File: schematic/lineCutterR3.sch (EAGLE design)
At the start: 53 parts, among them IC2 MC33269ST-3.3T3, J1 10118192-0001LF, Q1 AO4576, Q2 AO4576, Q3 DMG2305, Q4 AO4576, SW1 KMR2, U1 MS560702BA03-50, U2 MDBT50Q, U3 S25FL128SDPMFIG13S03016, U4 ESP32-S2-WROVER, U5 KXTJ3-1057, X1 2x5 0.05", X2 PIN-HEADER-MICRO-2-5-SMD

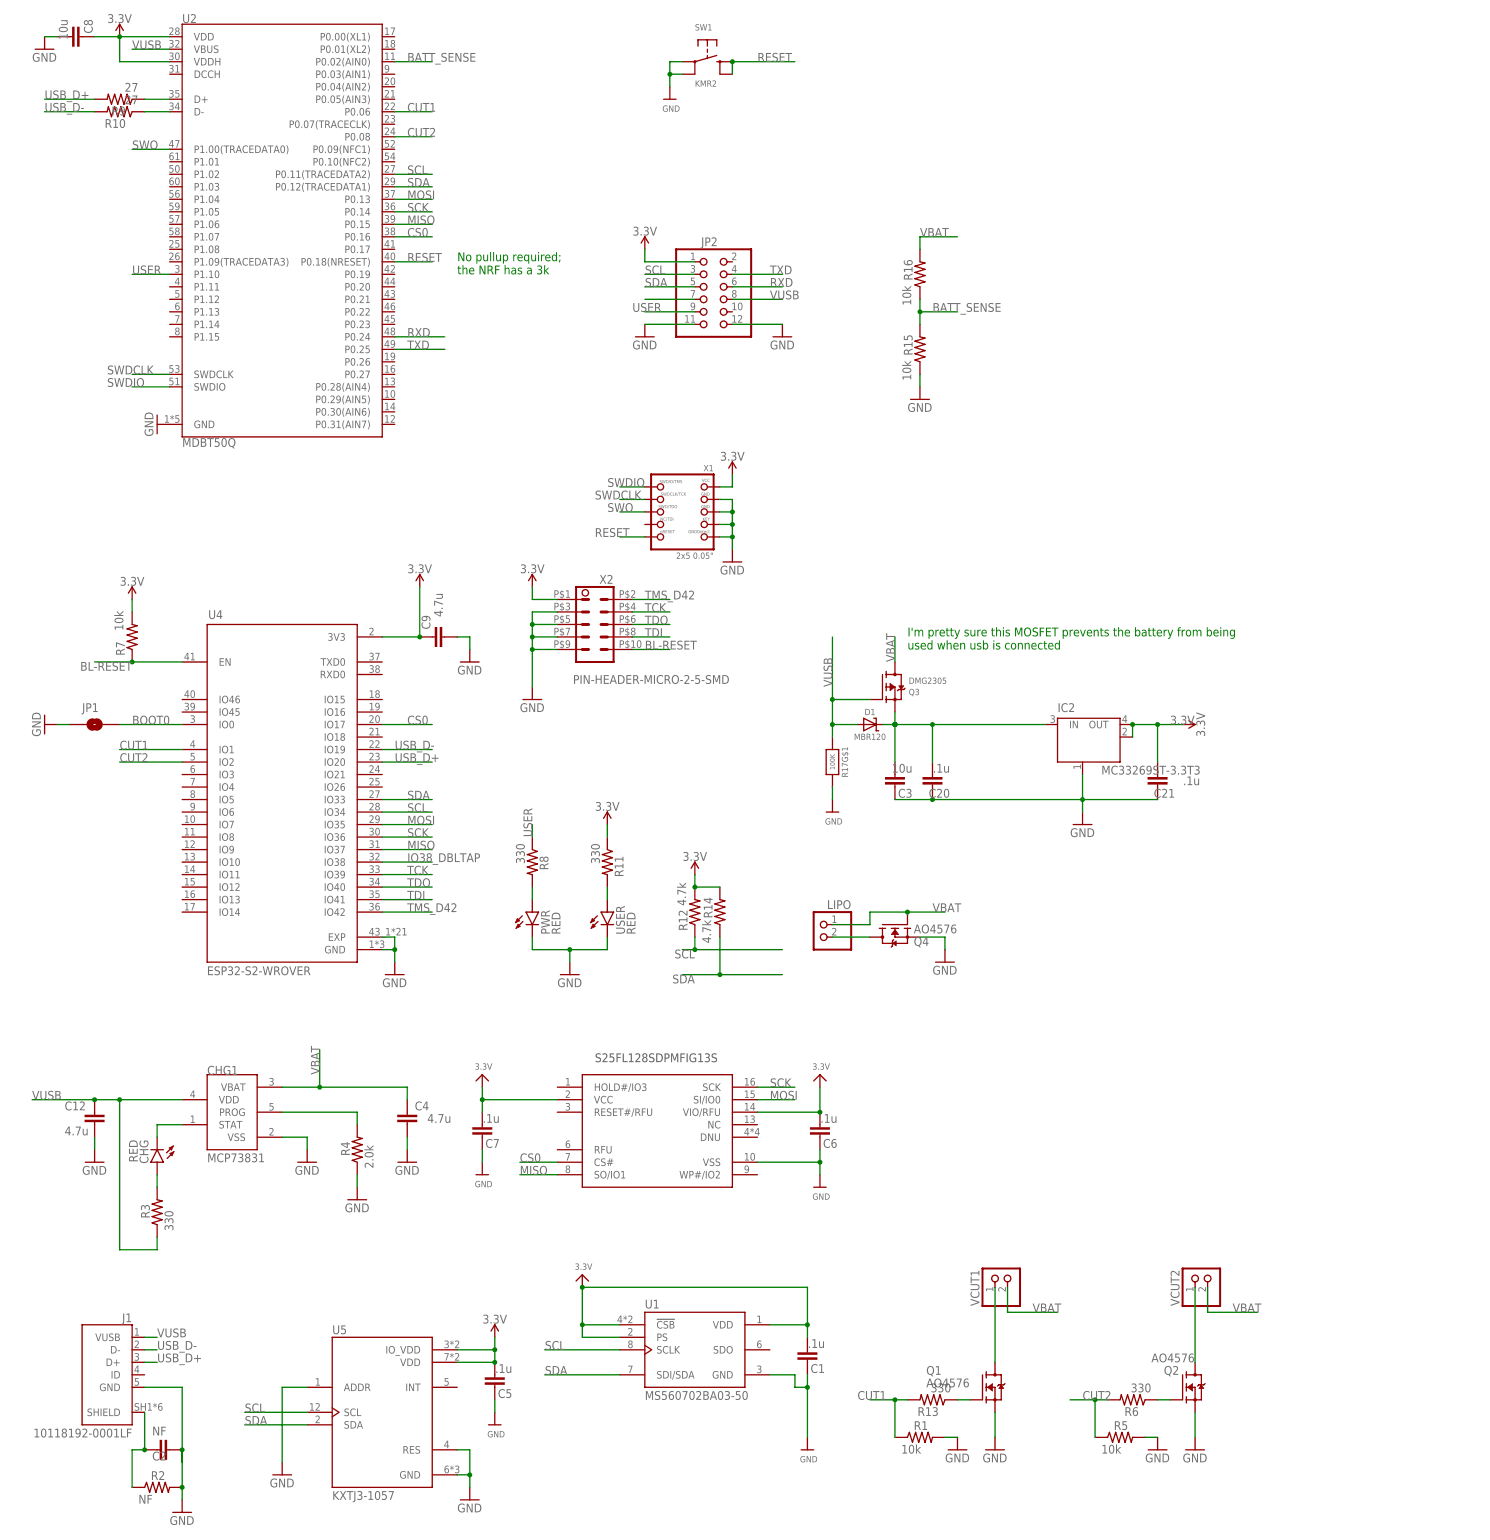
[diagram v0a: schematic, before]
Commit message: Add Buck/Boost, RGB, Continuity, current sense
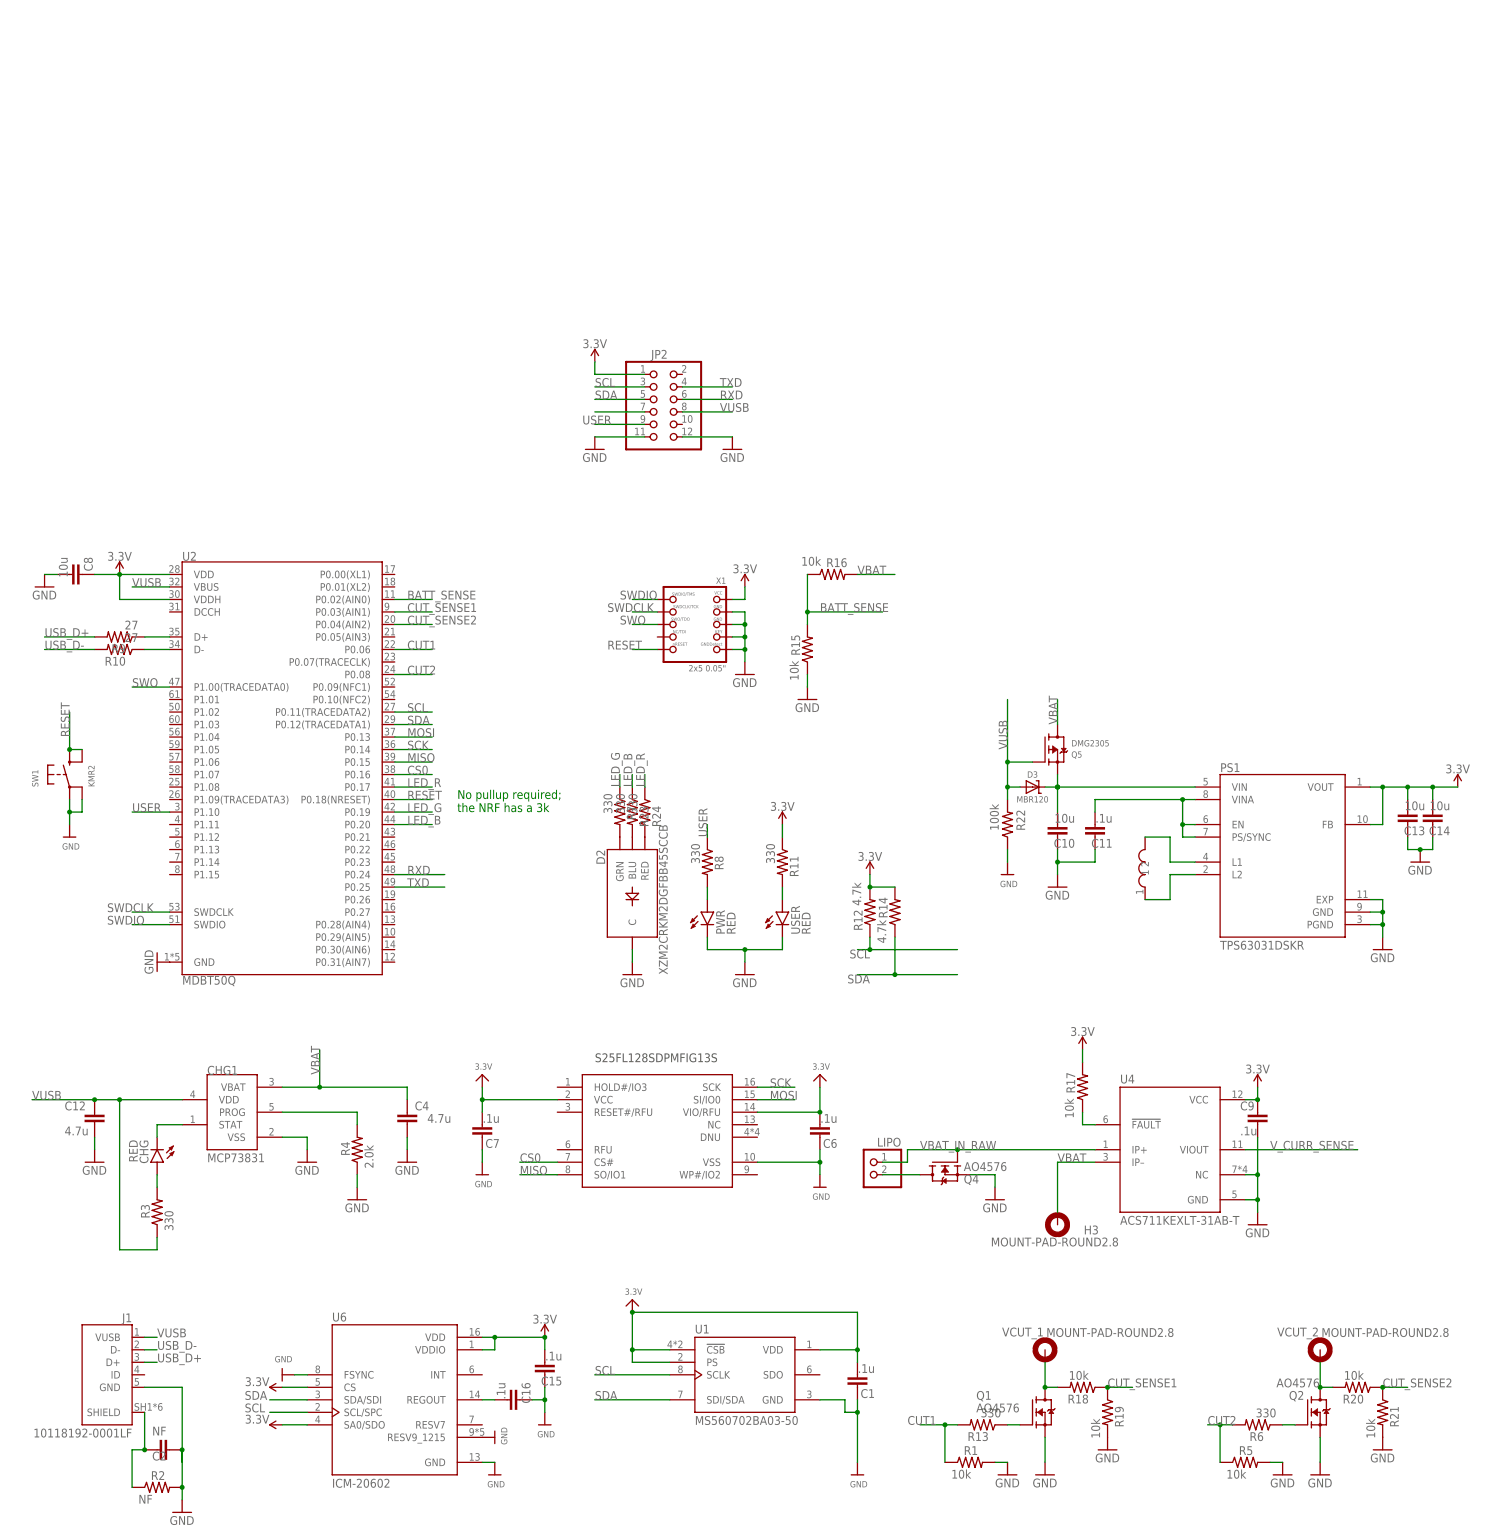
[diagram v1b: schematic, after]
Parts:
- removed C20, C21, C5: .1u, rcl:C-EUC0805
- removed C3: 10u, rcl:C-EUC0805
- removed D1: MBR120, microbuilder:DIODE-SCHOTTKYSOD-123
- removed IC2: MC33269ST-3.3T3, linear:MC33269ST-3.3T3
- removed JP1: JUMPER-SMT_2_NO_SILK, SparkFun-Jumpers:JUMPER-SMT_2_NO_SILK
- removed Q3: DMG2305, microbuilder:MOSFET-P
- removed U5: KXTJ3-1057, Line Cutter COTS:KXTJ3-1057
- removed VCUT1, VCUT2: (no value), pinhead:PINHD-1X2
- removed X2: PIN-HEADER-MICRO-2-5-SMD, freescale-uc:PIN-HEADER-MICRO-2-5-SMD
- added C10, C13, C14: 10u, rcl:C-EUC0805
- added C11, C15, C16: .1u, rcl:C-EUC0805
- added D2: XZM2CRKM2DGFBB45SCCB, SparkFun-LED:SUNLEDSMD1
- added D3: MBR120, microbuilder:DIODE-SCHOTTKYSOD-123
- added H3, VCUT_1, VCUT_2: MOUNT-PAD-ROUND2.8, holes:MOUNT-PAD-ROUND2.8
- added L1: NR3015T1R5N, Line Cutter COTS:NR3015T1R5N
- added PS1: TPS63031DSKR, Line Cutter COTS:TPS63031DSKR
- added Q5: DMG2305, microbuilder:MOSFET-P
- added R18, R19, R20, R21: 10k, rcl:R-US_R0805
- added R22: 100k, rcl:R-US_R0805
- added R23, R24: 330, rcl:R-US_R0805
- added U6: ICM-20602, Line Cutter COTS:ICM-20602
- C9: value 4.7u -> .1u
- R17: value 100K -> 10k; device microbuilder:RESISTOR_4PACK -> rcl:R-US_R0805
- R7: value 10k -> 330
- U4: value ESP32-S2-WROVER -> ACS711KEXLT-31AB-T; device Line Cutter COTS:ESP32-S2-WROVER -> Line Cutter COTS:ACS711KEXLT-31AB-T
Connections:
- removed net BL-RESET: R7.1, U4.EN, X2.10
- removed net BOOT0: JP1.2, U4.IO0
- removed net IO38_DBLTAP: U4.IO38
- removed net TCK: U4.IO39, X2.4
- removed net TDI: U4.IO41, X2.8
- removed net TDO: U4.IO40, X2.6
- removed net TMS_D42: U4.IO42, X2.2
- removed net VHI: C20.2, C3.2, D1.C, IC2.IN, Q3.S
- new net CUT_SENSE1: R18.1, R19.1, U2.P0.03(AIN1)
- new net CUT_SENSE2: R20.1, R21.1, U2.P0.04(AIN2)
- new net LED_B: R23.1, U2.P0.20
- new net LED_G: R7.1, U2.P0.19
- new net LED_R: R24.1, U2.P0.17
- new net N$14: R17.1, U4.!FAULT
- new net N$15: D2.GRN, R7.2
- new net N$17: Q1.D, R18.2, VCUT_1.MOUNT
- new net N$18: C11.2, PS1.EN, PS1.PS/SYNC, PS1.VINA
- new net N$19: L1.2, PS1.L1
- new net N$20: L1.1, PS1.L2
- new net N$21: D2.RED, R24.2
- new net N$22: C16.2, U6.REGOUT
- new net VBAT_IN_RAW: LIPO.1, Q4.G, U4.IP+
- new net VIN_REG1: C10.2, D3.C, PS1.VIN, Q5.S
- new net V_CURR_SENSE: U4.VIOUT
- net 3.3V: now also C13.2, C14.2, C15.2, PS1.FB, PS1.VOUT, R17.2, U4.VCC, U6.CS, U6.SA0/SDO, U6.VDD, U6.VDDIO; no longer C21.2, C5.2, IC2.OUT, IC2.OUT@1, R7.2, U4.3V3, U5.IO_VDD, U5.VDD, X2.1
- net CS0: no longer U4.IO17
- net CUT1: no longer U4.IO1
- net CUT2: no longer U4.IO2
- net GND: now also C10.1, C11.1, C13.1, C14.1, C15.1, C16.1, D2.C, PS1.EXP, PS1.GND, PS1.PGND, R19.2, R21.2, R22.1, U4.NC, U6.FSYNC, U6.GND, U6.RESV9_1215; no longer C20.1, C21.1, C3.1, C5.1, IC2.GND/ADJ, JP1.1, R17G$1.2, U4.EXP, U5.ADDR, U5.GND, U5.RES, X2.3, X2.5, X2.7, X2.9
- net MISO: no longer U4.IO37
- net MOSI: no longer U4.IO35
- net N$16: now also D2.BLU, R23.2; no longer Q1.D, VCUT1.1
- net N$6: now also R20.2, VCUT_2.MOUNT; no longer VCUT2.1
- net SCK: no longer U4.IO36
- net SCL: now also U6.SCL/SPC; no longer U4.IO34, U5.SCL
- net SDA: now also U6.SDA/SDI; no longer U4.IO33, U5.SDA
- net USB_D+: no longer U4.IO20
- net USB_D-: no longer U4.IO19
- net VBAT: now also H3.MOUNT, Q5.D, U4.IP–; no longer LIPO.1, Q3.D, Q4.G, VCUT1.2, VCUT2.2
- net VUSB: now also D3.A, Q5.G, R22.2; no longer D1.A, Q3.G, R17G$1.1
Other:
- note removed: "I'm pretty sure this MOSFET prevents the battery from being used when usb is connected"
- moved on the sheet: C1, C8, C9, JP2, LIPO, PWR, Q1, Q2, Q4, R1, R10, R11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
